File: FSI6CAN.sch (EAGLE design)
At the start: 39 parts, among them IC2 TCAN332DR, IC3 ATMEGA328P, IC4 MCP2515

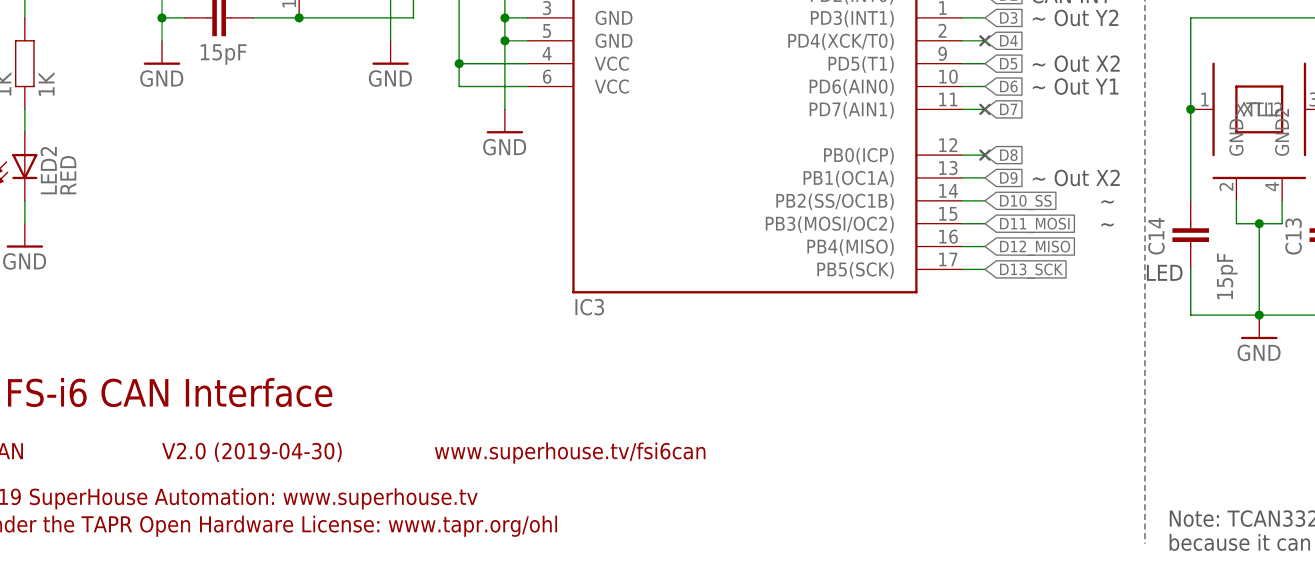
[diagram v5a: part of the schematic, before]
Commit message: Fixed silkscreen labels for outputs and for MCU orientation
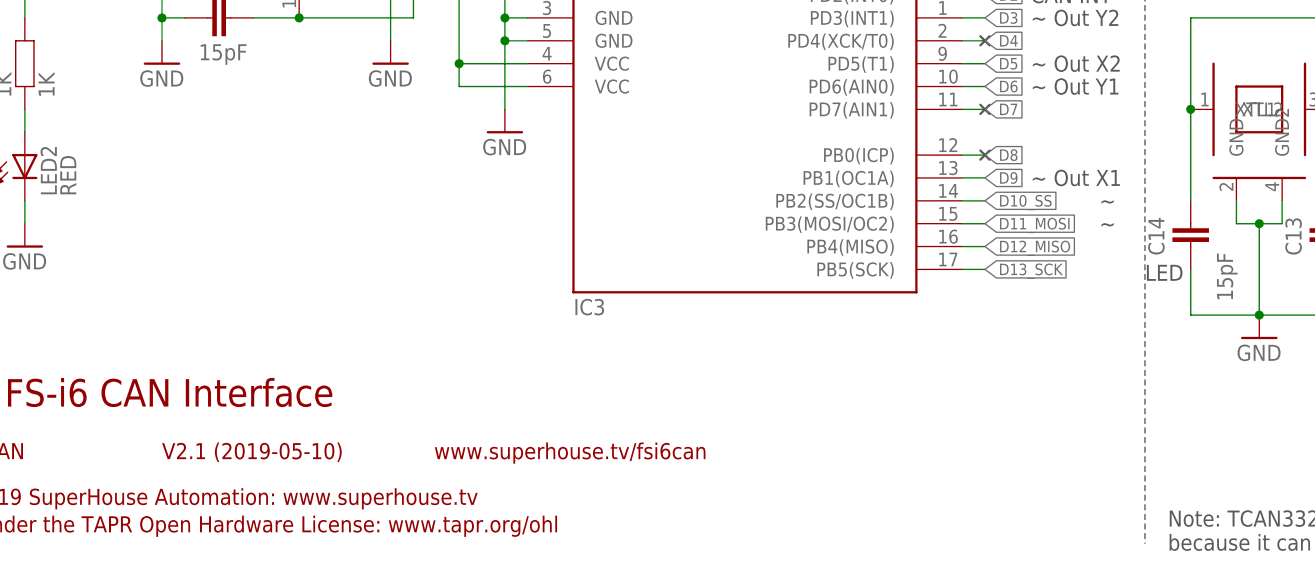
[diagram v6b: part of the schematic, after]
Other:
- note added: "V2.1 (2019-05-10)"
- note added: "~ Out X1"
- note removed: "V2.0 (2019-04-30)"
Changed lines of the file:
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@@
 <text x="10.16" y="127" size="2.54" layer="94" ratio="12">ATmega32m1 MCU</text>
 <text x="7.62" y="20.32" size="3.048" layer="94">Flysky FS-i6 CAN Interface</text>
-<text x="38.1" y="14.478" size="1.778" layer="94">V2.0 (2019-04-30)</text>
+<text x="38.1" y="14.478" size="1.778" layer="94">V2.1 (2019-05-10)</text>
 <text x="7.62" y="14.478" size="1.778" layer="94">SKU: FSI6CAN</text>
 <text x="7.366" y="9.398" size="1.778" layer="94">(C)2018-2019 SuperHouse Automation: www.superhouse.tv</text>
@@
 because it can operate at 3.3V</text>
 <text x="134.62" y="66.04" size="1.778" layer="97" align="center-left">CAN INT</text>
-<text x="134.62" y="45.72" size="1.778" layer="97" align="center-left">~ Out X2</text>
+<text x="134.62" y="45.72" size="1.778" layer="97" align="center-left">~ Out X1</text>
 <text x="142.24" y="43.18" size="1.778" layer="97" align="center-left">~</text>
 <text x="142.24" y="40.64" size="1.778" layer="97" align="center-left">~</text>

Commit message: Part replacement using SuperHouse libraries
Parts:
- 1K: device freetronics-jon:RESISTOR0603 -> SuperHouse-DiscreteSemi:RESISTOR0603
- C1, C10, C11, C13, C14, C3, C5, C6, C9: device freetronics-master-v1.1:CAP0603 -> SuperHouse-DiscreteSemi:CAP0603
- R1, R17, R2, R3, R4, R9: device freetronics-master-v1.1:RESISTOR0603 -> SuperHouse-DiscreteSemi:RESISTOR0603
- S21: device freetronics-jon:TAC_SWITCH_2PINSMT -> SuperHouse-Switches:TAC_SWITCH_2PINSMT

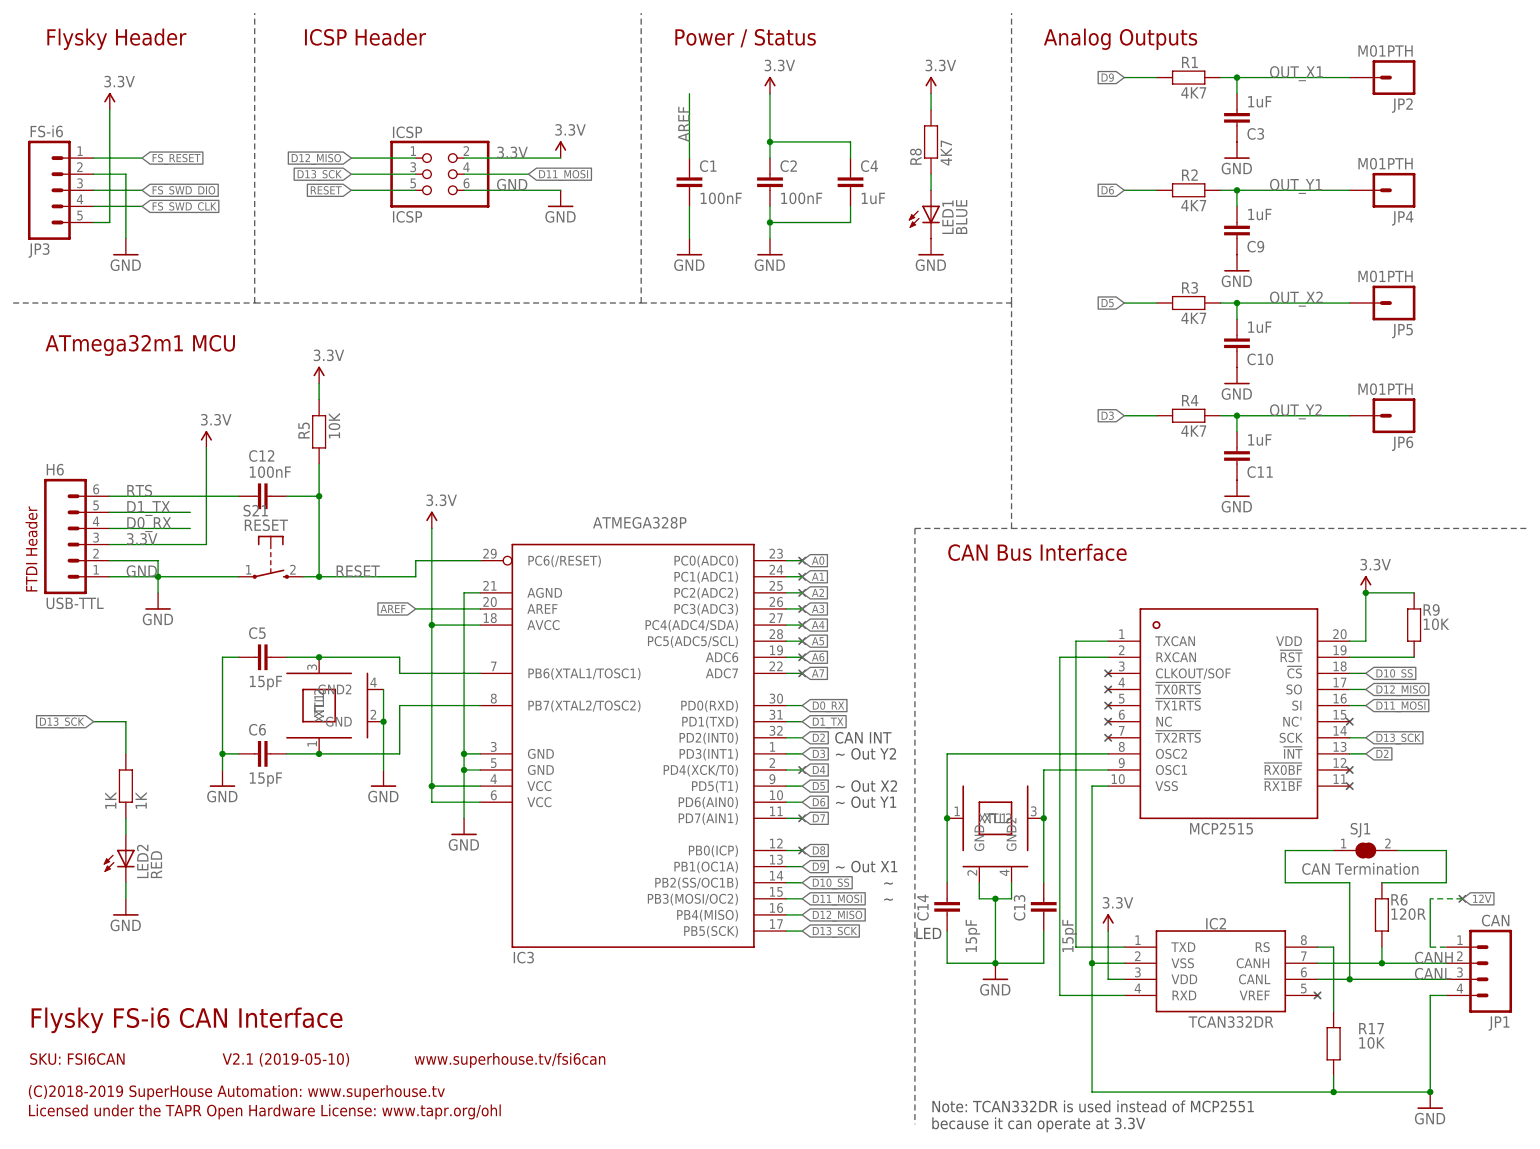
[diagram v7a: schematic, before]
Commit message: Part replacement using SuperHouse libraries
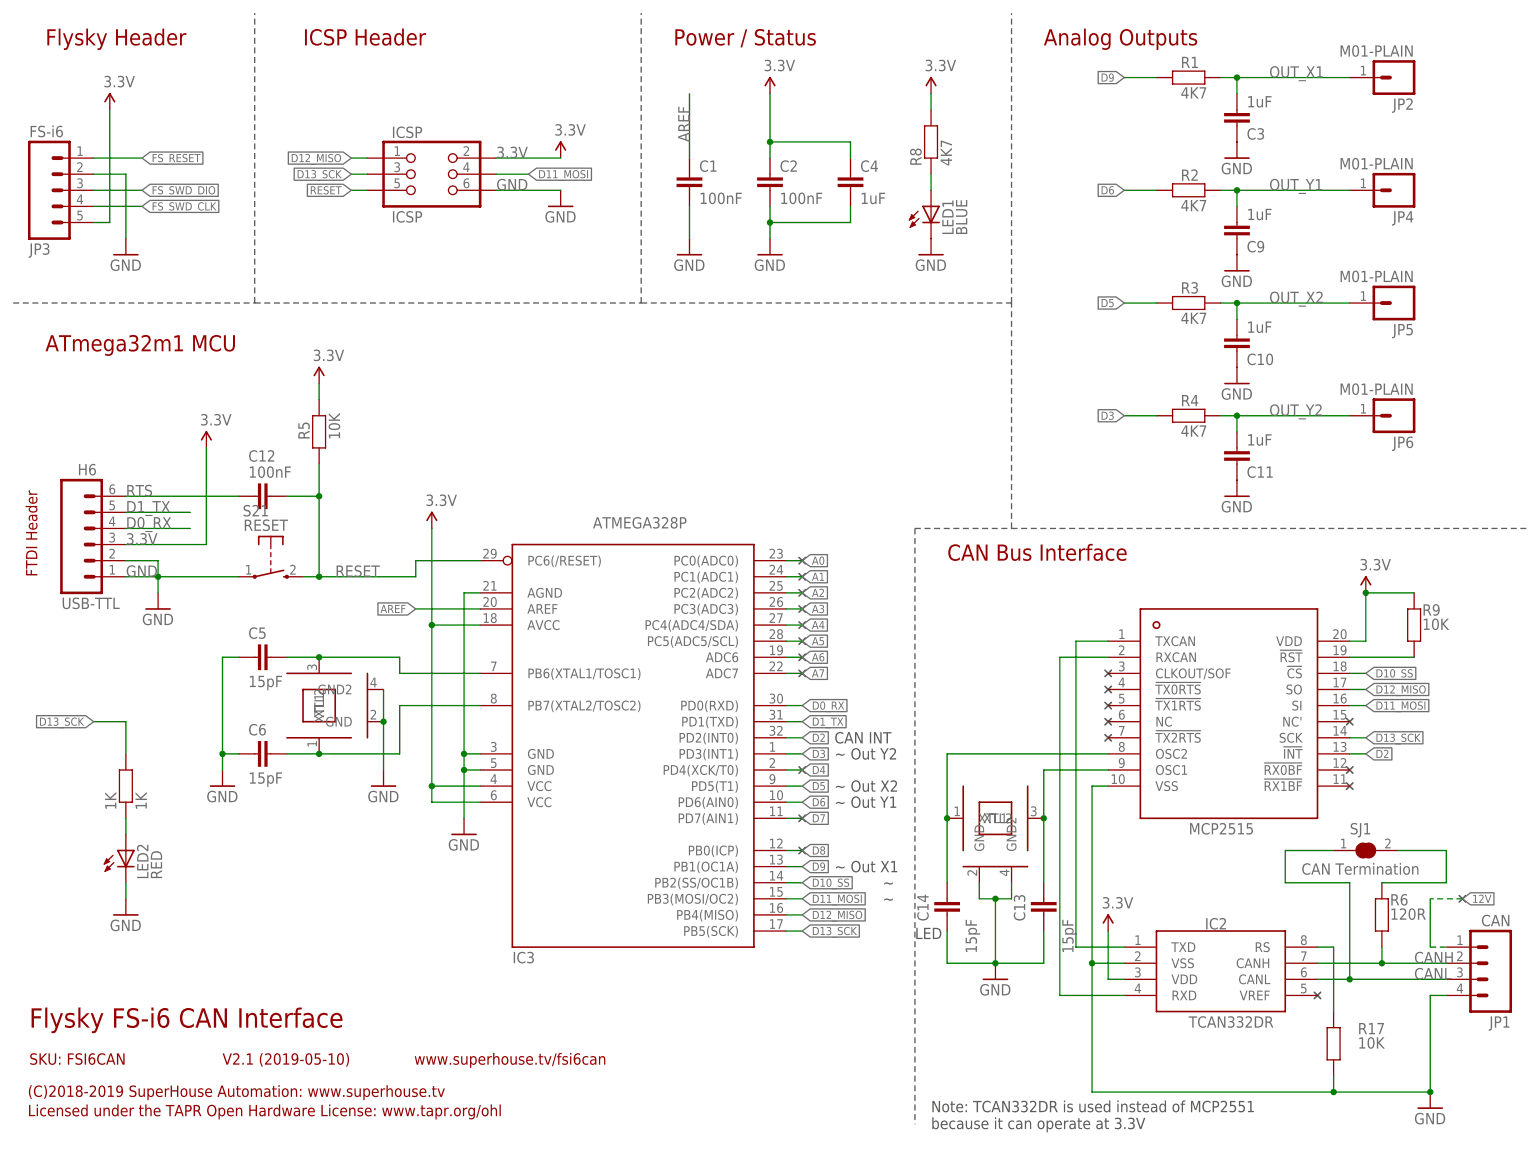
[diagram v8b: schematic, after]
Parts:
- C12, C2, C4: device freetronics-master-v1.1:CAP0603 -> SuperHouse-DiscreteSemi:CAP0603
- H6: device freetronics:M06SIP -> SuperHouse-Connectors:M06-PIN-RIGHTANGLE
- IC2: device freetronics-original:MCP2551 -> SuperHouse-ICs:MCP2551
- IC3: device freetronics-master-v1.1:AVR-MEGA8-AI -> SuperHouse-MCUs:ATMEGA8-AI
- IC4: device MCP2515:MCP2515 -> SuperHouse-ICs:MCP2515
- ICSP: device pinhead:PINHD-2X3 -> SuperHouse-Connectors:ICSP-PIN
- JP1: device freetronics-jon:M04PTH -> SuperHouse-Connectors:M04-PIN
- JP2, JP4, JP5, JP6: value M01PTH -> M01-PLAIN; device freetronics-jon:M01PTH -> SuperHouse-Connectors:M01-PLAIN
- LED1, LED2: device freetronics-jon:LED0603 -> SuperHouse-LEDs:LED0603
- R5, R6: device freetronics-master-v1.1:RESISTOR0603 -> SuperHouse-DiscreteSemi:RESISTOR0603
- R8: device freetronics-jon:RESISTOR0603 -> SuperHouse-DiscreteSemi:RESISTOR0603
- SJ1: device freetronics-jon:SJCN -> SuperHouse-Jumpers:SJC-NORMAL
- XTL1, XTL3: device freetronics-jon:CRYSTAL-GND3X2 -> SuperHouse-Oscillators:CRYSTAL-GND3X2
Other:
- moved on the sheet: H6
